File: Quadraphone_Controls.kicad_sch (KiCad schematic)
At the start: 20 parts, among them J1 Conn_01x10_Female, J10 Pitch_In, J11 Mix_Out, J12 Conn_02x04_Top_Bottom, J13 Conn_01x04_Male, J14 Conn_01x01_Male, J2 Conn_01x10_Female, J3 Conn_01x10_Female, J4 Conn_01x10_Female, J5 PWM_CV, J6 LFO_IN, J7 PWM_CV_In, J8 Synch_Signal_In, J9 Freq_Mod_In, SW1 Synch_Type, SW2 Output_Type

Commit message: Clean up control board
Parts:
- added D1: 3d_Model_Components, Custom_Footprints:3D_Dummy, symbol Mountjoy:3d_Model_Dummy
- added D2: 3d_Model_Panel, Custom_Footprints:3D_Dummy, symbol Mountjoy:3d_Model_Dummy

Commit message: Added readme
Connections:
- net MIX_OUT2: now also J11.2; no longer J11.3
- net MIX_OUT3: now also J11.3; no longer J11.2
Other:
- note added: "v3.0 fixes: Mix out 2 and 3 reversed"
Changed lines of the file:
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@@
   (title_block
     (title "Quadraphone Controls")
-    (date "2023-03-02")
-    (rev "2.0")
+    (date "2023-03-19")
+    (rev "3.0")
     (company "Mountjoy Modular")
   )
@@
   )
   (text "v2.0 fixes:\nOutput type switch mirrored in X plane\nEthernet connections incorrectly mapped\nAdded interconnects for V/Oct and Mix Out"
-    (at 238.76 177.8 0)
+    (at 237.49 177.8 0)
+    (effects (font (size 1.27 1.27)) (justify left bottom))
+  )
+  (text "v3.0 fixes:\nMix out 2 and 3 reversed" (at 182.88 172.72 0)
     (effects (font (size 1.27 1.27)) (justify left bottom))
   )
@@
     (effects (font (size 1.27 1.27)) (justify left bottom))
   )
-  (label "MIX_OUT3" (at 256.54 149.86 0)
+  (label "MIX_OUT3" (at 256.54 147.32 0)
     (effects (font (size 1.27 1.27)) (justify left bottom))
   )
@@
     (effects (font (size 1.27 1.27)) (justify left bottom))
   )
-  (label "MIX_OUT2" (at 256.54 147.32 0)
-    (effects (font (size 1.27 1.27)) (justify left bottom))
-  )
+  (label "MIX_OUT2" (at 256.54 149.86 0)
+    (effects (font (size 1.27 1.27)) (justify left bottom))
+  )

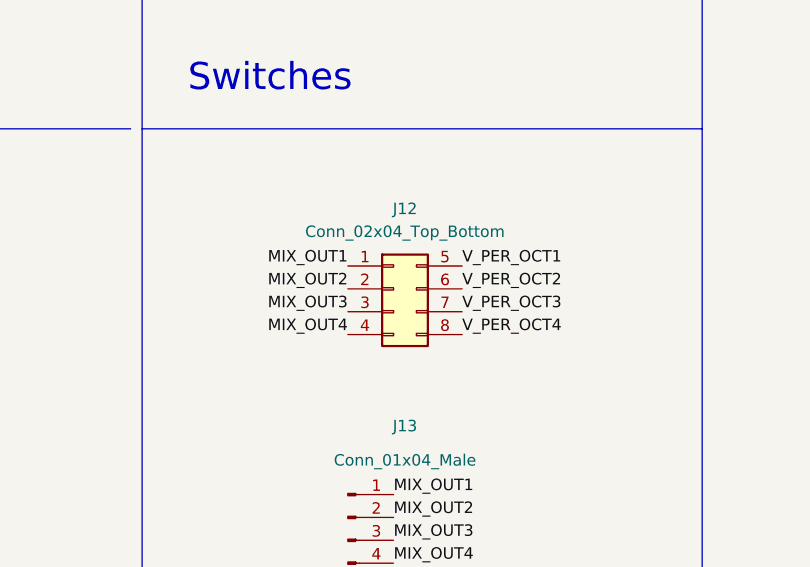
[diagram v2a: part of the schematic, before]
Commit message: Fixes to footprints on controls board
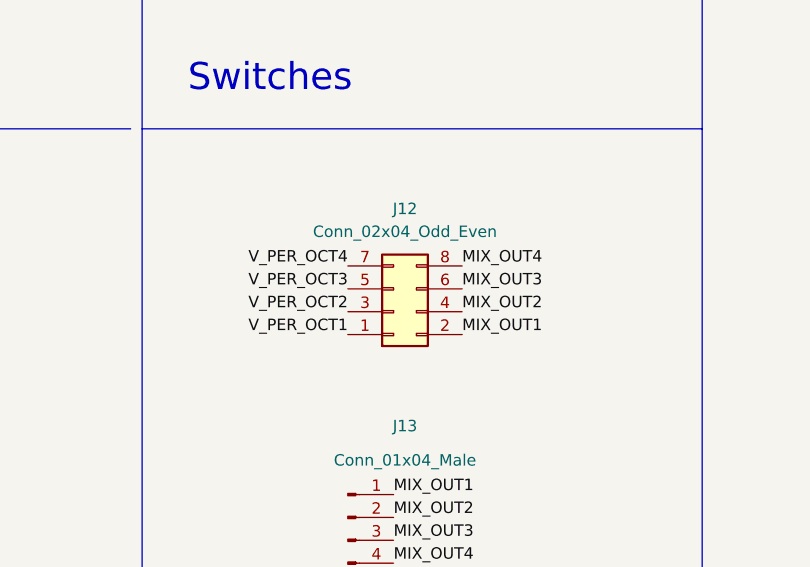
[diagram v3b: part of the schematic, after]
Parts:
- removed J12: Conn_02x04_Top_Bottom, Connector_PinHeader_2.54mm:PinHeader_2x04_P2.54mm_Vertical, symbol Connector_Generic:Conn_02x04_Top_Bottom
- added J12: Conn_02x04_Odd_Even, Connector_PinHeader_2.54mm:PinHeader_2x04_P2.54mm_Vertical, symbol Connector_Generic:Conn_02x04_Odd_Even
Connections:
- net MIX_OUT1: now also J12.2 (Pin_2)
- net MIX_OUT2: now also J12.4 (Pin_4)
- net MIX_OUT3: now also J12.6 (Pin_6)
- net MIX_OUT4: now also J12.8 (Pin_8)
- net V_PER_OCT1: now also J12.1 (Pin_1)
- net V_PER_OCT2: now also J12.3 (Pin_3)
- net V_PER_OCT3: now also J12.5 (Pin_5)
- net V_PER_OCT4: now also J12.7 (Pin_7)

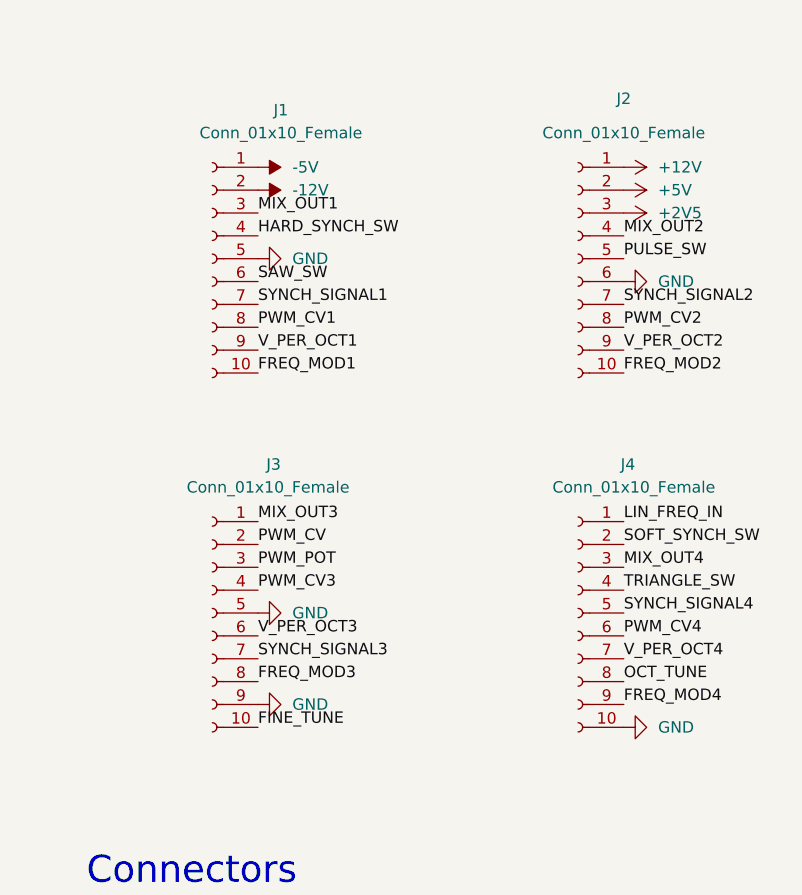
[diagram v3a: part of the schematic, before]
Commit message: Updates to v3; changed output mix feedback resistors to lower output level
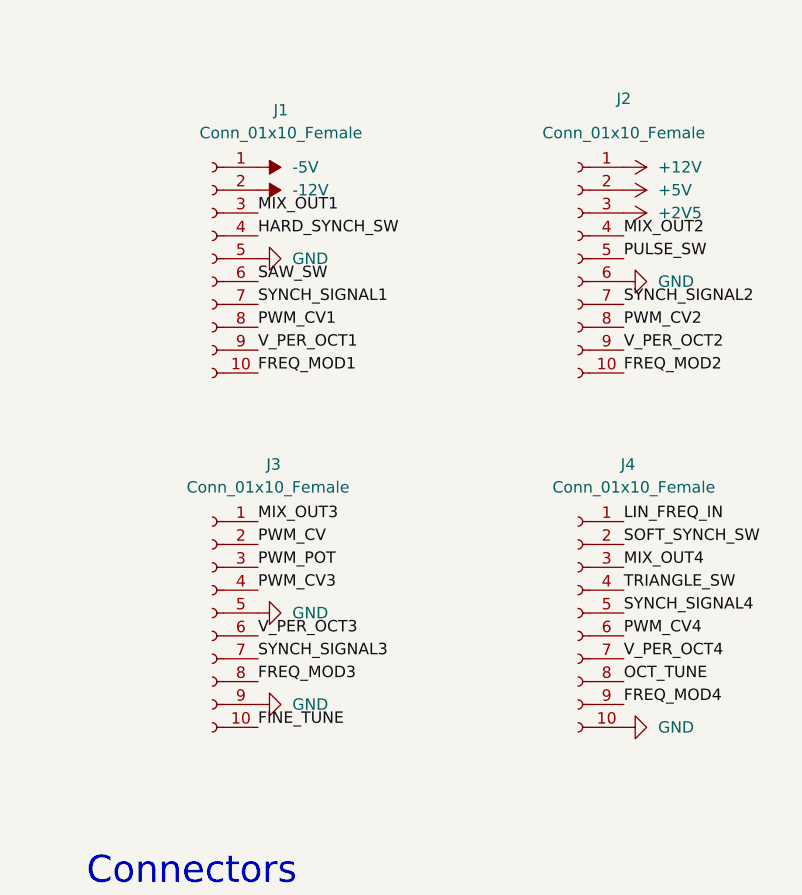
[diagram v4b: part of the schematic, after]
